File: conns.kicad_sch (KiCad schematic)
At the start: 5 parts, among them J1 GSB1C4621DS1HR

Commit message: finishing mcu design schematic
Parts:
- added J2: M20-8770546 (for SWD), Connector_PinSocket_2.54mm:PinSocket_1x05_P2.54mm_Vertical, symbol Connector:Conn_01x05_Pin
- added J3: M20-8770342 (for RasPi), Connector_PinSocket_2.54mm:PinSocket_1x03_P2.54mm_Vertical, symbol Connector:Conn_01x03_Pin
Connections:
- net GND: now also J2.3 (Pin_3), J3.3 (Pin_3)
- new net ST_JTCLK: J2.2 (Pin_2)
- new net ST_JTMS/SWDIO: J2.4 (Pin_4)
- new net ST_NRST: J2.5 (Pin_5)
- new net SW_USART2_RX: J3.2 (Pin_2)
- new net SW_USART2_TX: J3.1 (Pin_1)
- new net VDD: J2.1 (Pin_1)
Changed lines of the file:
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@@
+    (stroke (width 0) (type default))
+  )
+  (wire (pts (xy 59.69 142.24) (xy 72.39 142.24))
     (stroke (width 0) (type default))
   )
@@
     (stroke (width 0) (type default))
   )
+  (wire (pts (xy 59.69 144.78) (xy 63.5 144.78))
+    (stroke (width 0) (type default))
+  )
   (wire (pts (xy 92.71 45.72) (xy 92.71 48.26))
     (stroke (width 0) (type default))
@@
     (stroke (width 0) (type default))
   )
+  (wire (pts (xy 64.77 106.68) (xy 64.77 97.79))
+    (stroke (width 0) (type default))
+  )
+  (wire (pts (xy 55.88 114.3) (xy 63.5 114.3))
+    (stroke (width 0) (type default))
+  )
   (wire (pts (xy 54.61 45.72) (xy 59.69 45.72))
     (stroke (width 0) (type default))
@@
     (stroke (width 0) (type default))
   )
+  (wire (pts (xy 55.88 116.84) (xy 63.5 116.84))
+    (stroke (width 0) (type default))
+  )
   (wire (pts (xy 25.4 66.04) (xy 34.29 66.04))
     (stroke (width 0) (type default))
@@
     (stroke (width 0) (type default))
   )
+  (wire (pts (xy 59.69 139.7) (xy 72.39 139.7))
+    (stroke (width 0) (type default))
+  )
   (wire (pts (xy 58.42 35.56) (xy 58.42 54.61))
     (stroke (width 0) (type default))
@@
     (stroke (width 0) (type default))
   )
+  (wire (pts (xy 55.88 109.22) (xy 63.5 109.22))
+    (stroke (width 0) (type default))
+  )
+  (wire (pts (xy 55.88 111.76) (xy 59.69 111.76))
+    (stroke (width 0) (type default))
+  )
   (wire (pts (xy 40.64 38.1) (xy 55.88 38.1))
     (stroke (width 0) (type default))
@@
     (stroke (width 0) (type default))
   )
+  (wire (pts (xy 59.69 111.76) (xy 59.69 120.65))
+    (stroke (width 0) (type default))
+  )
+  (wire (pts (xy 55.88 106.68) (xy 64.77 106.68))
+    (stroke (width 0) (type default))
+  )
   (wire (pts (xy 40.64 50.8) (xy 40.64 66.04))
     (stroke (width 0) (type default))
@@
   (wire (pts (xy 92.71 48.26) (xy 92.71 50.8))
     (stroke (width 0) (type default))
+  )
+  (wire (pts (xy 63.5 144.78) (xy 63.5 152.4))
+    (stroke (width 0) (type default))
+  )
+  (global_label "ST_JTMS{slash}SWDIO" (shape bidirectional) (at 63.5 114.3 0) (fields_autoplaced)
+    (effects (font (size 1.27 1.27)) (justify left))
+    (property "Intersheetrefs" "${INTERSHEET_REFS}" (at 82.534 114.3 0)
+      (effects (font (size 1.27 1.27)) (justify left) hide)
+    )
   )
   (global_label "GS_VBUS" (shape bidirectional) (at 55.88 31.75 180) (fields_autoplaced)
@@
     )
   )
+  (global_label "VDD" (shape bidirectional) (at 64.77 97.79 0) (fields_autoplaced)
+    (effects (font (size 1.27 1.27)) (justify left))
+    (property "Intersheetrefs" "${INTERSHEET_REFS}" (at 72.4951 97.79 0)
+      (effects (font (size 1.27 1.27)) (justify left) hide)
+    )
+  )
+  (global_label "SW_USART2_TX" (shape bidirectional) (at 72.39 139.7 0) (fields_autoplaced)
+    (effects (font (size 1.27 1.27)) (justify left))
+    (property "Intersheetrefs" "${INTERSHEET_REFS}" (at 90.3354 139.7 0)
+      (effects (font (size 1.27 1.27)) (justify left) hide)
+    )
+  )
   (global_label "D+" (shape bidirectional) (at 54.61 43.18 180) (fields_autoplaced)
     (effects (font (size 1.27 1.27)) (justify right))
@@
     )
   )
+  (global_label "ST_NRST" (shape bidirectional) (at 63.5 116.84 0) (fields_autoplaced)
+    (effects (font (size 1.27 1.27)) (justify left))
+    (property "Intersheetrefs" "${INTERSHEET_REFS}" (at 75.5188 116.84 0)
+      (effects (font (size 1.27 1.27)) (justify left) hide)
+    )
+  )
+  (global_label "SW_USART2_RX" (shape bidirectional) (at 72.39 142.24 0) (fields_autoplaced)
+    (effects (font (size 1.27 1.27)) (justify left))
+    (property "Intersheetrefs" "${INTERSHEET_REFS}" (at 90.6378 142.24 0)
+      (effects (font (size 1.27 1.27)) (justify left) hide)
+    )
+  )
+  (global_label "ST_JTCLK" (shape bidirectional) (at 63.5 109.22 0) (fields_autoplaced)
+    (effects (font (size 1.27 1.27)) (justify left))
+    (property "Intersheetrefs" "${INTERSHEET_REFS}" (at 76.2445 109.22 0)
+      (effects (font (size 1.27 1.27)) (justify left) hide)
+    )
+  )
   (global_label "D-" (shape bidirectional) (at 92.71 40.64 0) (fields_autoplaced)
     (effects (font (size 1.27 1.27)) (justify left))
@@
     )
   )
+  (symbol (lib_id "power:GND") (at 63.5 152.4 0) (unit 1)
+    (in_bom yes) (on_board yes) (dnp no) (fields_autoplaced)
+    (property "Reference" "#PWR056" (at 63.5 158.75 0)
+      (effects (font (size 1.27 1.27)) hide)
+    )
+    (property "Value" "GND" (at 63.5 157.48 0)
+      (effects (font (size 1.27 1.27)))
+    )
+    (property "Footprint" "" (at 63.5 152.4 0)
+      (effects (font (size 1.27 1.27)) hide)
+    )
+    (property "Datasheet" "" (at 63.5 152.4 0)
+      (effects (font (size 1.27 1.27)) hide)
+    )
+    (pin "1")
+    (instances
+      (project "radar2"
+        (path "/4b235fed-a05d-46ae-99fd-4a907d865754/dfc10a02-f047-425a-8f9d-e4a822e029f8"
+          (reference "#PWR056") (unit 1)
+        )
+      )
+    )
+  )
   (symbol (lib_id "Device:C_Small") (at 36.83 66.04 90) (unit 1)
     (in_bom yes) (on_board yes) (dnp no) (fields_autoplaced)
@@
         (path "/4b235fed-a05d-46ae-99fd-4a907d865754/dfc10a02-f047-425a-8f9d-e4a822e029f8"
           (reference "R8") (unit 1)
+        )
+      )
+    )
+  )
+  (symbol (lib_id "Connector:Conn_01x03_Pin") (at 54.61 142.24 0) (unit 1)
+    (in_bom yes) (on_board yes) (dnp no) (fields_autoplaced)
+    (property "Reference" "J3" (at 55.245 134.62 0)
+      (effects (font (size 1.27 1.27)))
+    )
+    (property "Value" "M20-8770342 (for RasPi)" (at 55.245 137.16 0)
+      (effects (font (size 1.27 1.27)))
+    )
+    (property "Footprint" "Connector_PinSocket_2.54mm:PinSocket_1x03_P2.54mm_Vertical" (at 54.61 142.24 0)
+      (effects (font (size 1.27 1.27)) hide)
+    )
+    (property "Datasheet" "~" (at 54.61 142.24 0)
+      (effects (font (size 1.27 1.27)) hide)
+    )
+    (pin "3")
+    (pin "1")
+    (pin "2")
+    (instances
+      (project "radar2"
+        (path "/4b235fed-a05d-46ae-99fd-4a907d865754/dfc10a02-f047-425a-8f9d-e4a822e029f8"
+          (reference "J3") (unit 1)
+        )
+      )
+    )
+  )
+  (symbol (lib_id "Connector:Conn_01x05_Pin") (at 50.8 111.76 0) (unit 1)
+    (in_bom yes) (on_board yes) (dnp no) (fields_autoplaced)
+    (property "Reference" "J2" (at 51.435 101.6 0)
+      (effects (font (size 1.27 1.27)))
+    )
+    (property "Value" "M20-8770546 (for SWD)" (at 51.435 104.14 0)
+      (effects (font (size 1.27 1.27)))
+    )
+    (property "Footprint" "Connector_PinSocket_2.54mm:PinSocket_1x05_P2.54mm_Vertical" (at 50.8 111.76 0)
+      (effects (font (size 1.27 1.27)) hide)
+    )
+    (property "Datasheet" "~" (at 50.8 111.76 0)
+      (effects (font (size 1.27 1.27)) hide)
+    )
+    (pin "4")
+    (pin "2")
+    (pin "5")
+    (pin "1")
+    (pin "3")
+    (instances
+      (project "radar2"
+        (path "/4b235fed-a05d-46ae-99fd-4a907d865754/dfc10a02-f047-425a-8f9d-e4a822e029f8"
+          (reference "J2") (unit 1)
         )
       )
@@
         )
       )
+    )
+  )
+  (symbol (lib_id "power:GND") (at 59.69 120.65 0) (unit 1)
+    (in_bom yes) (on_board yes) (dnp no) (fields_autoplaced)
+    (property "Reference" "#PWR053" (at 59.69 127 0)
+      (effects (font (size 1.27 1.27)) hide)
+    )
+    (property "Value" "GND" (at 59.69 125.73 0)
+      (effects (font (size 1.27 1.27)))
+    )
+    (property "Footprint" "" (at 59.69 120.65 0)
+      (effects (font (size 1.27 1.27)) hide)
+    )
+    (property "Datasheet" "" (at 59.69 120.65 0)
+      (effects (font (size 1.27 1.27)) hide)
+    )
+    (pin "1")
+    (instances
+      (project "radar2"
+        (path "/4b235fed-a05d-46ae-99fd-4a907d865754/dfc10a02-f047-425a-8f9d-e4a822e029f8"
+          (reference "#PWR053") (unit 1)
+        )
+      )

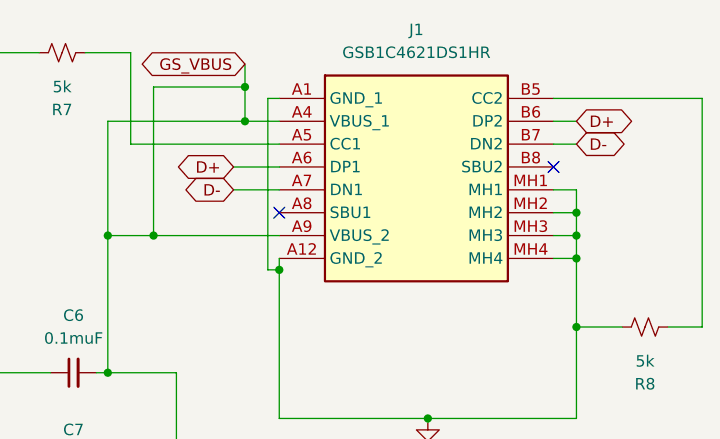
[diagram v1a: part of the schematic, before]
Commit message: no connects on mcu and D+, D- on connector, ILIM_HIZ voltage divider controls input current
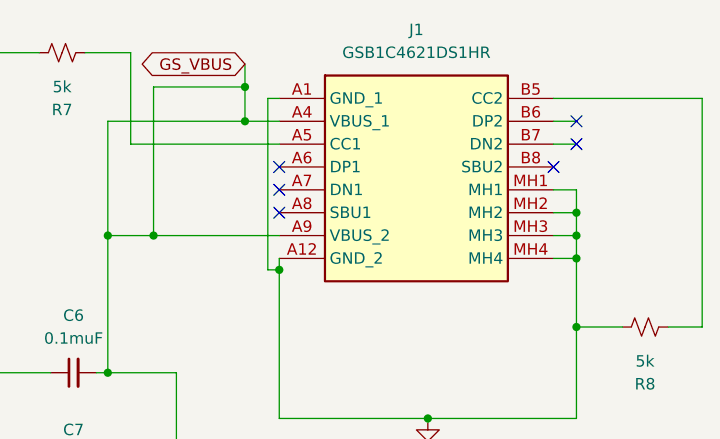
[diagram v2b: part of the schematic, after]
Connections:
- net D+: no longer names the net of J1.A6 (DP1)
- net D+: no longer J1.B6 (DP2)
- net D-: no longer names the net of J1.A7 (DN1)
- net D-: no longer J1.B7 (DN2)
- no-connect marks 2 -> 6
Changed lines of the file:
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@@
   )
   (no_connect (at 59.69 48.26))
+  (no_connect (at 92.71 38.1))
+  (no_connect (at 92.71 40.64))
   (no_connect (at 90.17 43.18))
+  (no_connect (at 59.69 45.72))
+  (no_connect (at 59.69 43.18))
   (wire (pts (xy 40.64 66.04) (xy 48.26 66.04))
     (stroke (width 0) (type default))
@@
     (stroke (width 0) (type default))
   )
-  (wire (pts (xy 54.61 43.18) (xy 59.69 43.18))
-    (stroke (width 0) (type default))
-  )
   (wire (pts (xy 39.37 78.74) (xy 48.26 78.74))
     (stroke (width 0) (type default))
@@
   )
   (wire (pts (xy 55.88 114.3) (xy 63.5 114.3))
-    (stroke (width 0) (type default))
-  )
-  (wire (pts (xy 54.61 45.72) (xy 59.69 45.72))
     (stroke (width 0) (type default))
   )
@@
     )
   )
-  (global_label "D+" (shape bidirectional) (at 54.61 43.18 180) (fields_autoplaced)
-    (effects (font (size 1.27 1.27)) (justify right))
-    (property "Intersheetrefs" "${INTERSHEET_REFS}" (at 47.6711 43.18 0)
-      (effects (font (size 1.27 1.27)) (justify right) hide)
-    )
-  )
   (global_label "VBUS" (shape bidirectional) (at 48.26 86.36 0) (fields_autoplaced)
     (effects (font (size 1.27 1.27)) (justify left))
@@
     )
   )
-  (global_label "D-" (shape bidirectional) (at 54.61 45.72 180) (fields_autoplaced)
-    (effects (font (size 1.27 1.27)) (justify right))
-    (property "Intersheetrefs" "${INTERSHEET_REFS}" (at 47.6711 45.72 0)
-      (effects (font (size 1.27 1.27)) (justify right) hide)
-    )
-  )
-  (global_label "D+" (shape bidirectional) (at 92.71 38.1 0) (fields_autoplaced)
-    (effects (font (size 1.27 1.27)) (justify left))
-    (property "Intersheetrefs" "${INTERSHEET_REFS}" (at 99.6489 38.1 0)
-      (effects (font (size 1.27 1.27)) (justify left) hide)
-    )
-  )
   (global_label "ST_NRST" (shape bidirectional) (at 63.5 116.84 0) (fields_autoplaced)
     (effects (font (size 1.27 1.27)) (justify left))
@@
       (effects (font (size 1.27 1.27)) (justify left) hide)
     )
-  )
-  (global_label "D-" (shape bidirectional) (at 92.71 40.64 0) (fields_autoplaced)
-    (effects (font (size 1.27 1.27)) (justify left))
-    (property "Intersheetrefs" "${INTERSHEET_REFS}" (at 99.6489 40.64 0)
-      (effects (font (size 1.27 1.27)) (justify left) hide)
-    )

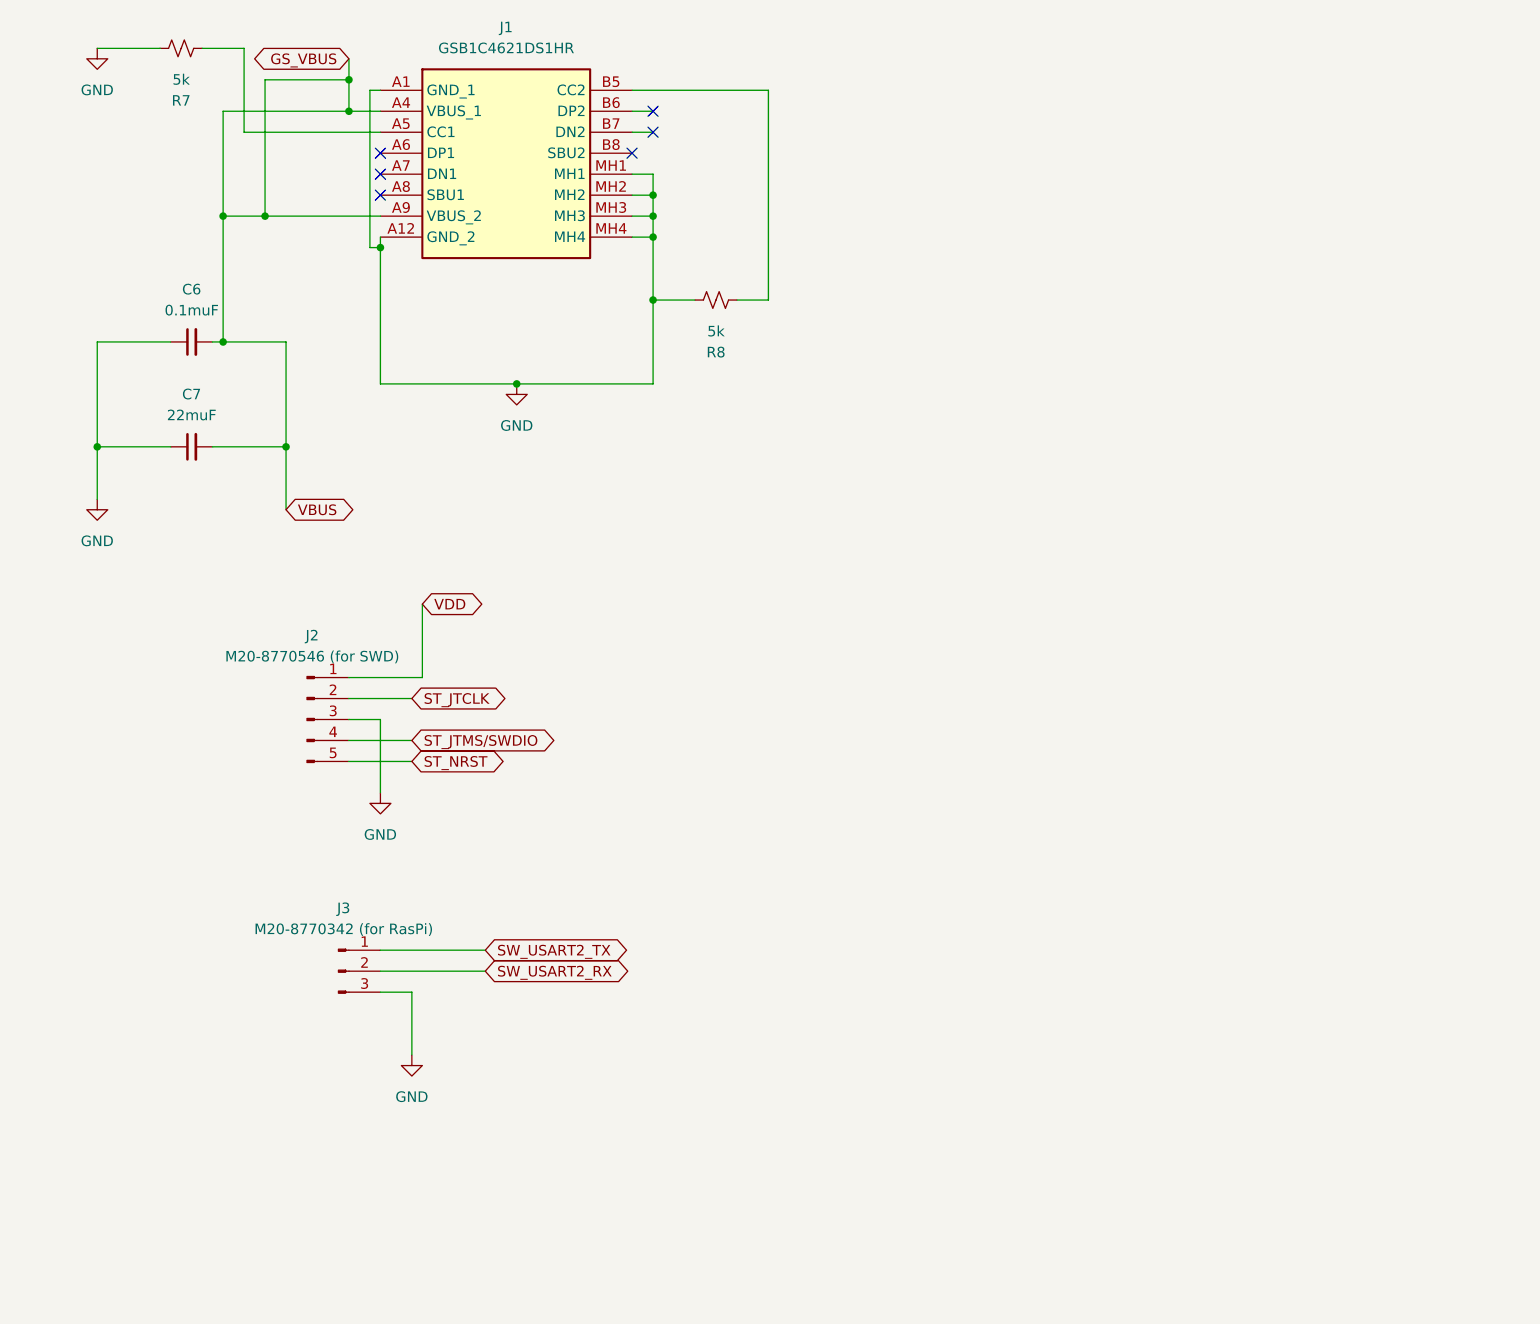
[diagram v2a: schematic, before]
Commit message: fixed GS_VBUS overtaking the GND symbol error, lesson learned, fixed PCB ratnest
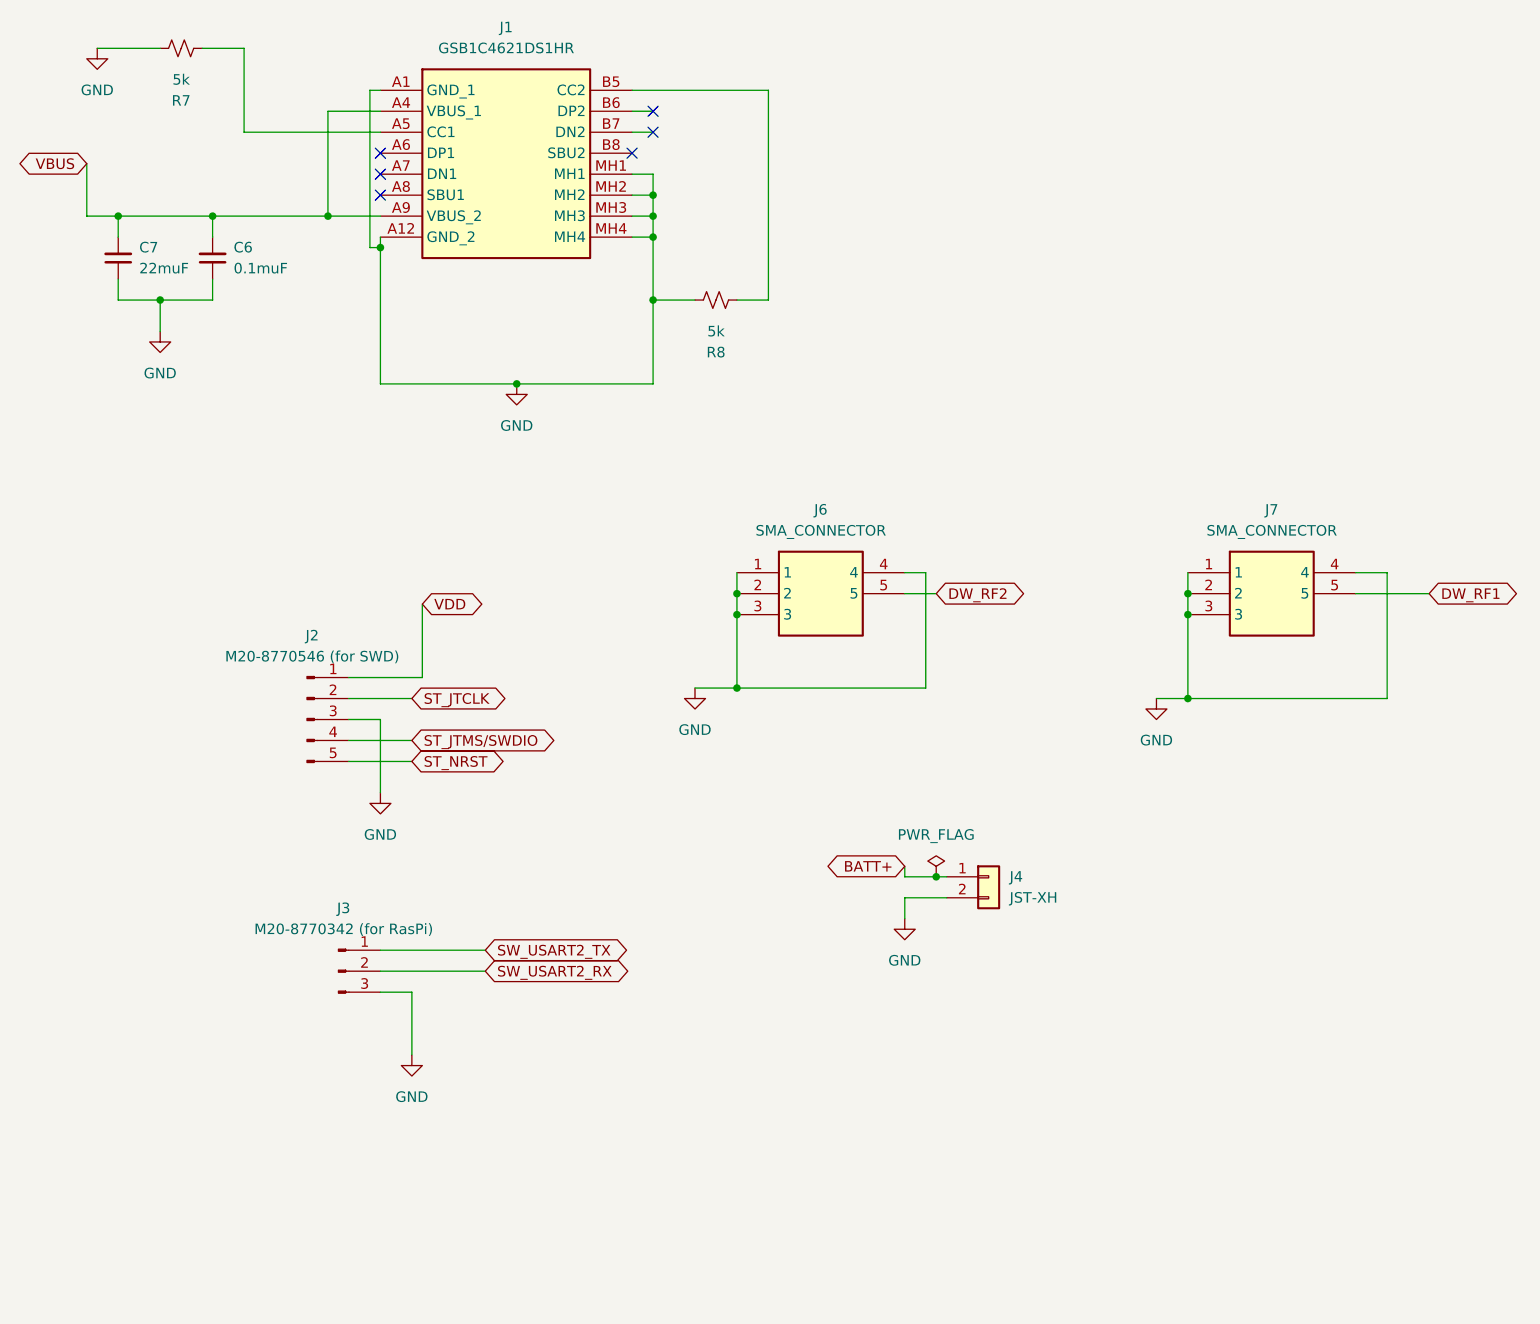
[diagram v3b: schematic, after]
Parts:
- added J4: JST-XH, Connector_JST:JST_XH_B2B-XH-AM_1x02_P2.50mm_Vertical, symbol Connector_Generic:Conn_01x02
- added J6, J7: SMA_CONNECTOR, sma_conn1:SMACONNECTOR, symbol sma_conn1:SMA_CONNECTOR
- J1: footprint USB_C2:GSB -> gsb_usb:GSB
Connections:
- net GND: now also J4.2 (Pin_2), J6.1, J6.2, J6.3, J6.4, J7.1, J7.2, J7.3, J7.4
- net GS_VBUS renamed VBUS
- new net BATT+: J4.1 (Pin_1)
- new net DW_RF1: J7.5
- new net DW_RF2: J6.5
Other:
- moved on the sheet: C6, C7
